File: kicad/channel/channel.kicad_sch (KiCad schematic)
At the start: 42 parts, among them J1 Conn_01x07_Male, J5V1 Conn_01x01_Male, Q1 BC846B, Q2 IRF3205, Q3 IRF3205, Q4 BC846B, Q5 IRF3205, Q6 IRF3205, U1 LM324

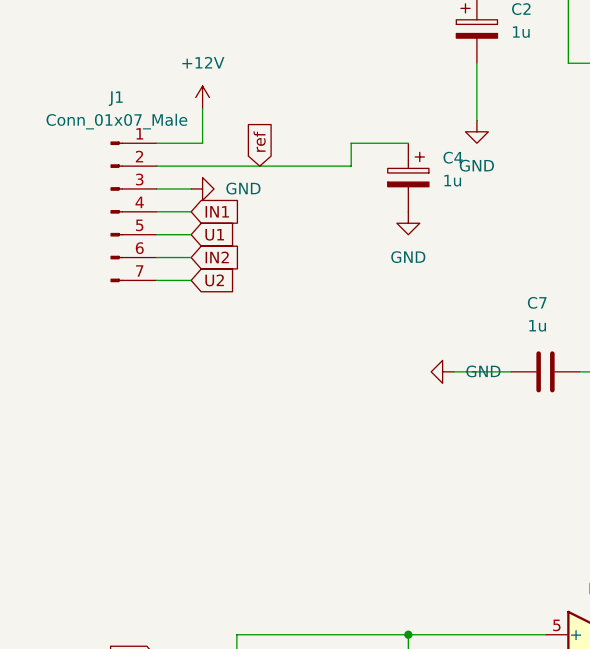
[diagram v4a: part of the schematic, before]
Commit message: move mosfets
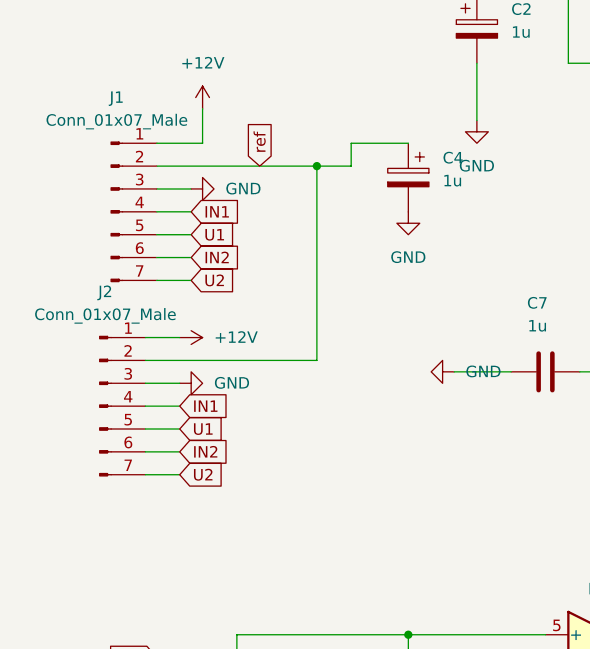
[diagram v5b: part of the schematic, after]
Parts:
- added J2: Conn_01x07_Male, Connector_PinHeader_2.54mm:PinHeader_1x07_P2.54mm_Vertical, symbol Connector:Conn_01x07_Male
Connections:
- net +12V: now also J2.1 (Pin_1)
- net GND: now also J2.3 (Pin_3)
- net IN1: now also J2.4 (Pin_4)
- net IN2: now also J2.6 (Pin_6)
- net U1: now also J2.5 (Pin_5)
- net U2: now also J2.7 (Pin_7)
- net ref: now also J2.2 (Pin_2)
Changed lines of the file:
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@@
   (junction (at 128.27 33.02) (diameter 0) (color 0 0 0 0)
   )
+  (junction (at 44.45 95.25) (diameter 0) (color 0 0 0 0)
+  )
   (junction (at 162.56 87.63) (diameter 0) (color 0 0 0 0)
   )
@@
     (stroke (width 0) (type default) (color 0 0 0 0))
   )
+  (wire (pts (xy 25.4 114.3) (xy 29.21 114.3))
+    (stroke (width 0) (type default) (color 0 0 0 0))
+  )
   (wire (pts (xy 146.05 55.88) (xy 146.05 60.96))
     (stroke (width 0) (type default) (color 0 0 0 0))
@@
     (stroke (width 0) (type default) (color 0 0 0 0))
   )
+  (wire (pts (xy 25.4 127) (xy 29.21 127))
+    (stroke (width 0) (type default) (color 0 0 0 0))
+  )
   (wire (pts (xy 194.31 149.86) (xy 121.92 149.86))
     (stroke (width 0) (type default) (color 0 0 0 0))
@@
     (stroke (width 0) (type default) (color 0 0 0 0))
   )
+  (wire (pts (xy 25.4 119.38) (xy 29.21 119.38))
+    (stroke (width 0) (type default) (color 0 0 0 0))
+  )
   (wire (pts (xy 62.23 71.12) (xy 77.47 71.12))
     (stroke (width 0) (type default) (color 0 0 0 0))
@@
     (stroke (width 0) (type default) (color 0 0 0 0))
   )
+  (wire (pts (xy 44.45 116.84) (xy 25.4 116.84))
+    (stroke (width 0) (type default) (color 0 0 0 0))
+  )
   (wire (pts (xy 207.01 90.17) (xy 207.01 87.63))
     (stroke (width 0) (type default) (color 0 0 0 0))
@@
     (stroke (width 0) (type default) (color 0 0 0 0))
   )
-  (wire (pts (xy 26.67 95.25) (xy 48.26 95.25))
+  (wire (pts (xy 25.4 124.46) (xy 29.21 124.46))
+    (stroke (width 0) (type default) (color 0 0 0 0))
+  )
+  (wire (pts (xy 26.67 95.25) (xy 44.45 95.25))
     (stroke (width 0) (type default) (color 0 0 0 0))
   )
@@
     (stroke (width 0) (type default) (color 0 0 0 0))
   )
+  (wire (pts (xy 25.4 129.54) (xy 29.21 129.54))
+    (stroke (width 0) (type default) (color 0 0 0 0))
+  )
   (wire (pts (xy 54.61 92.71) (xy 48.26 92.71))
     (stroke (width 0) (type default) (color 0 0 0 0))
@@
     (stroke (width 0) (type default) (color 0 0 0 0))
   )
+  (wire (pts (xy 44.45 95.25) (xy 48.26 95.25))
+    (stroke (width 0) (type default) (color 0 0 0 0))
+  )
   (wire (pts (xy 69.85 152.4) (xy 64.77 152.4))
     (stroke (width 0) (type default) (color 0 0 0 0))
@@
     (stroke (width 0) (type default) (color 0 0 0 0))
   )
+  (wire (pts (xy 44.45 95.25) (xy 44.45 116.84))
+    (stroke (width 0) (type default) (color 0 0 0 0))
+  )
   (wire (pts (xy 167.64 121.92) (xy 173.99 121.92))
     (stroke (width 0) (type default) (color 0 0 0 0))
@@
   )
   (wire (pts (xy 100.33 30.48) (xy 100.33 55.88))
+    (stroke (width 0) (type default) (color 0 0 0 0))
+  )
+  (wire (pts (xy 25.4 121.92) (xy 29.21 121.92))
     (stroke (width 0) (type default) (color 0 0 0 0))
   )
@@
     )
   )
+  (global_label "U2" (shape input) (at 29.21 129.54 0) (fields_autoplaced)
+    (effects (font (size 1.27 1.27)) (justify left))
+    (property "Intersheet References" "${INTERSHEET_REFS}" (id 0) (at 34.1631 129.6194 0)
+      (effects (font (size 1.27 1.27)) (justify left) hide)
+    )
+  )
   (global_label "IN2" (shape input) (at 26.67 149.86 180) (fields_autoplaced)
     (effects (font (size 1.27 1.27)) (justify right))
@@
     )
   )
+  (global_label "U1" (shape input) (at 29.21 124.46 0) (fields_autoplaced)
+    (effects (font (size 1.27 1.27)) (justify left))
+    (property "Intersheet References" "${INTERSHEET_REFS}" (id 0) (at 34.1631 124.5394 0)
+      (effects (font (size 1.27 1.27)) (justify left) hide)
+    )
+  )
   (global_label "ref" (shape input) (at 85.09 135.89 90) (fields_autoplaced)
     (effects (font (size 1.27 1.27)) (justify left))
@@
     (property "Intersheet References" "${INTERSHEET_REFS}" (id 0) (at 28.7321 73.5806 0)
       (effects (font (size 1.27 1.27)) (justify right) hide)
+    )
+  )
+  (global_label "IN1" (shape input) (at 29.21 121.92 0) (fields_autoplaced)
+    (effects (font (size 1.27 1.27)) (justify left))
+    (property "Intersheet References" "${INTERSHEET_REFS}" (id 0) (at 34.7679 121.9994 0)
+      (effects (font (size 1.27 1.27)) (justify left) hide)
+    )
+  )
+  (global_label "IN2" (shape input) (at 29.21 127 0) (fields_autoplaced)
+    (effects (font (size 1.27 1.27)) (justify left))
+    (property "Intersheet References" "${INTERSHEET_REFS}" (id 0) (at 34.7679 127.0794 0)
+      (effects (font (size 1.27 1.27)) (justify left) hide)
     )
   )
@@
     (pin "1")
     (pin "2")
+  )
+  (symbol (lib_id "Connector:Conn_01x07_Male") (at 20.32 121.92 0) (unit 1)
+    (in_bom yes) (on_board yes) (fields_autoplaced)
+    (property "Reference" "J2" (id 0) (at 20.955 109.22 0))
+    (property "Value" "Conn_01x07_Male" (id 1) (at 20.955 111.76 0))
+    (property "Footprint" "Connector_PinHeader_2.54mm:PinHeader_1x07_P2.54mm_Vertical" (id 2) (at 20.32 121.92 0)
+      (effects (font (size 1.27 1.27)) hide)
+    )
+    (property "Datasheet" "~" (id 3) (at 20.32 121.92 0)
+      (effects (font (size 1.27 1.27)) hide)
+    )
+    (pin "1")
+    (pin "2")
+    (pin "3")
+    (pin "4")
+    (pin "5")
+    (pin "6")
+    (pin "7")
   )
   (symbol (lib_id "Device:R") (at 152.4 121.92 180) (unit 1)
@@
     (pin "2")
   )
+  (symbol (lib_id "power:+12V") (at 29.21 114.3 270) (unit 1)
+    (in_bom yes) (on_board yes) (fields_autoplaced)
+    (property "Reference" "#PWR0109" (id 0) (at 25.4 114.3 0)
+      (effects (font (size 1.27 1.27)) hide)
+    )
+    (property "Value" "+12V" (id 1) (at 33.02 114.2999 90)
+      (effects (font (size 1.27 1.27)) (justify left))
+    )
+    (property "Footprint" "" (id 2) (at 29.21 114.3 0)
+      (effects (font (size 1.27 1.27)) hide)
+    )
+    (property "Datasheet" "" (id 3) (at 29.21 114.3 0)
+      (effects (font (size 1.27 1.27)) hide)
+    )
+    (pin "1")
+  )
   (symbol (lib_id "Device:R") (at 135.89 43.18 0) (unit 1)
     (in_bom yes) (on_board yes) (fields_autoplaced)
@@
     (pin "1")
   )
+  (symbol (lib_id "power:GND") (at 29.21 119.38 90) (unit 1)
+    (in_bom yes) (on_board yes) (fields_autoplaced)
+    (property "Reference" "#PWR0108" (id 0) (at 35.56 119.38 0)
+      (effects (font (size 1.27 1.27)) hide)
+    )
+    (property "Value" "GND" (id 1) (at 33.02 119.3799 90)
+      (effects (font (size 1.27 1.27)) (justify right))
+    )
+    (property "Footprint" "" (id 2) (at 29.21 119.38 0)
+      (effects (font (size 1.27 1.27)) hide)
+    )
+    (property "Datasheet" "" (id 3) (at 29.21 119.38 0)
+      (effects (font (size 1.27 1.27)) hide)
+    )
+    (pin "1")
+  )
   (symbol (lib_id "Amplifier_Operational:LM324") (at 113.03 33.02 0) (unit 4)
     (in_bom yes) (on_board yes)
@@
       (reference "#PWR0107") (unit 1) (value "GND") (footprint "")
     )
+    (path "/ada2282f-55a8-4959-a24e-380ad62e4b4f"
+      (reference "#PWR0108") (unit 1) (value "GND") (footprint "")
+    )
+    (path "/7428d18f-8432-4ae9-ba14-fb004e868b00"
+      (reference "#PWR0109") (unit 1) (value "+12V") (footprint "")
+    )
     (path "/98bcbe84-6de1-4d54-8e02-faa40f5f06a1"
       (reference "C1") (unit 1) (value "1u") (footprint "Capacitor_SMD:C_0603_1608Metric")
@@
       (reference "J1") (unit 1) (value "Conn_01x07_Male") (footprint "Connector_PinHeader_2.54mm:PinHeader_1x07_P2.54mm_Vertical")
     )
+    (path "/2f7d50d8-5324-434b-8051-1263b8584a13"
+      (reference "J2") (unit 1) (value "Conn_01x07_Male") (footprint "Connector_PinHeader_2.54mm:PinHeader_1x07_P2.54mm_Vertical")
+    )
     (path "/1f8acd76-a450-4f1e-84f1-d90753458019"
